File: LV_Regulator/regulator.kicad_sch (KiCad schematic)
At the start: 46 parts, among them U5 BQ25858QWRRVRQ1, U6 CSD19506KTT, U7 CSD19506KTT, U8 CSD19506KTT, U9 CSD19506KTT

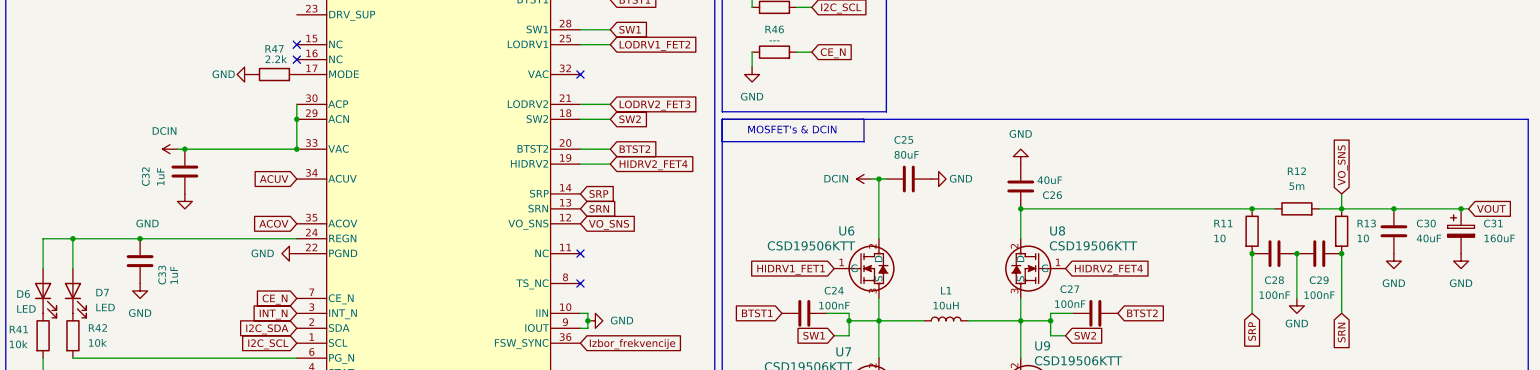
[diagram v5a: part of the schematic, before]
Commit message: Update to LV_Regulator schematic
Chosen some component's footprints as well as made a page for test points, etc.
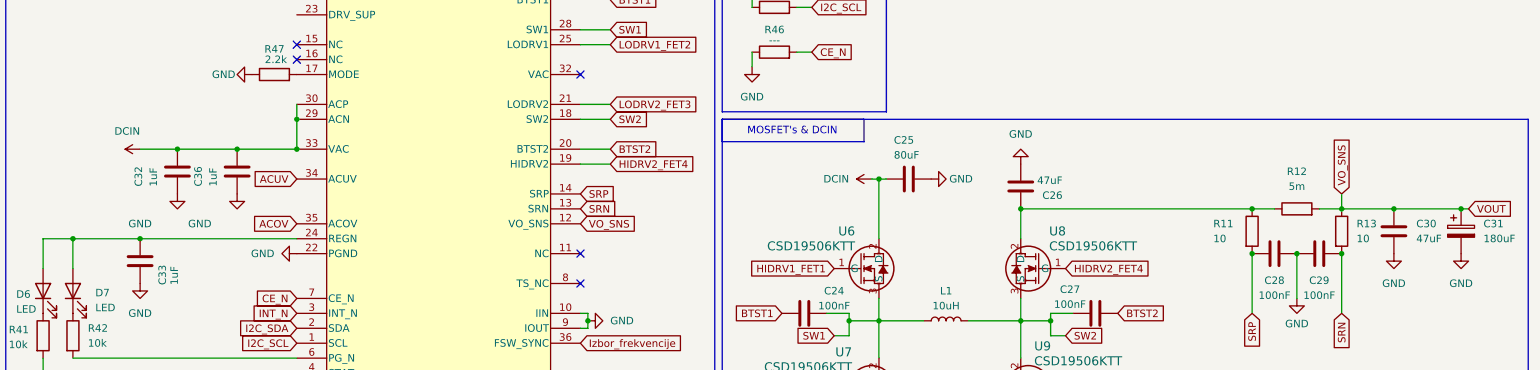
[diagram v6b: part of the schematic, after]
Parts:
- added C36: 1uF, Capacitor_SMD:C_1206_3216Metric, symbol Device:C
- C24, C27, C28: Purchase Place (none) -> https://www.digikey.com/en/products/detail/kemet/C1206C104K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
- C26, C30: value 40uF -> 47uF; footprint Capacitor_SMD:C_1206_3216Metric -> Capacitor_SMD:CP_Elec_10x10; Purchase Place (none) -> https://eu.mouser.com/ProductDetail/Vishay-BC-Components/MA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
- C29: Place of Purchase (none) -> https://www.digikey.com/en/products/detail/kemet/C1206C104K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
- C31: value 160uF -> 180uF; Buying Place (none) -> https://eu.mouser.com/ProductDetail/Nichicon/UCZ1J181MNS1MS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
- C32: Purchase place (none) -> https://eu.mouser.com/ProductDetail/KEMET/C1206C104K1RAC786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
- R12: footprint Resistor_SMD:R_1206_3216Metric -> FCSL110R005FER:RESC50110X70N; Purchase Place (none) -> https://eu.mouser.com/ProductDetail/Ohmite/FCSL110R005FER?q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
- R47: Purchase Place (none) -> https://eu.mouser.com/ProductDetail/ROHM-Semiconductor/ESR1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
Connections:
- net DCIN: now also C36.2
- net GND: now also C36.1
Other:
- moved on the sheet: C32

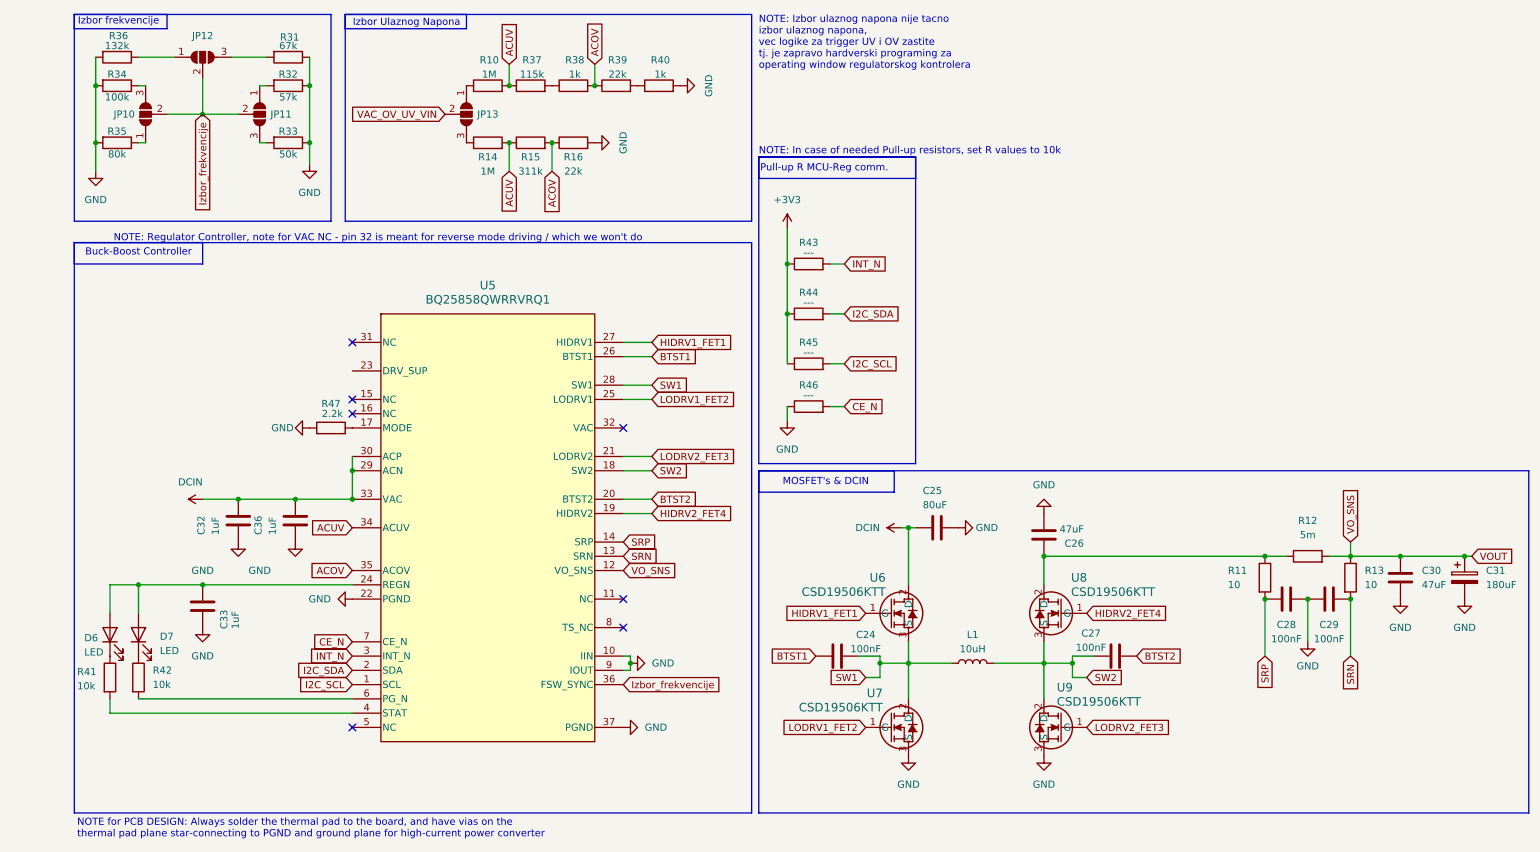
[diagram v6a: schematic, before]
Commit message: Multiple Updates
Added footprints and purchase links to the MCU page and updated some footprints on the Regulator Page from smd to SMD Handsolder
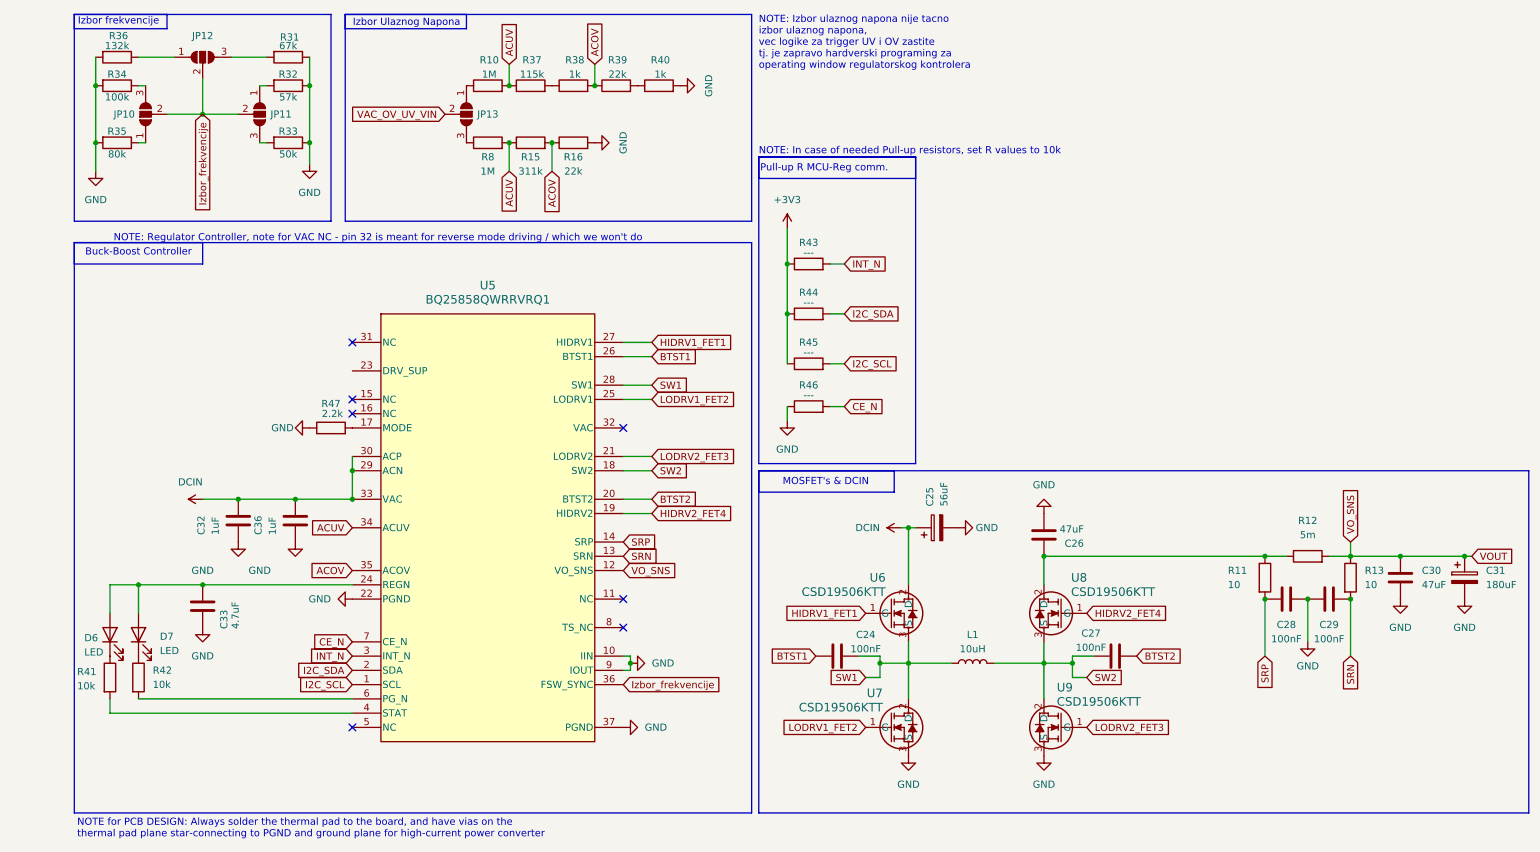
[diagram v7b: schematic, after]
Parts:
- removed C25: 80uF, Capacitor_SMD:C_1206_3216Metric, symbol Device:C
- removed R14: 1M, Resistor_SMD:R_1206_3216Metric, symbol Device:R
- added C25: 56uF, ul_UCZ1J181MNQ1MS:CAP_UCD_12P5X13P5_NCH, symbol Device:C_Polarized
- added R8: 1M, Resistor_SMD:R_1206_3216Metric_Pad1.30x1.75mm_HandSolder, symbol Device:R
- C33: value 1uF -> 4.7uF; Purchase Place (none) -> https://eu.mouser.com/ProductDetail/Walsin/SH31B475K250CT?q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
- D6, D7: Purchase Place (none) -> https://eu.mouser.com/ProductDetail/American-Bright-LED/BL-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
- JP10, JP12, JP13: footprint Jumper:SolderJumper-3_P1.3mm_Open_Pad1.0x1.5mm -> Jumper:SolderJumper-3_P1.3mm_Open_RoundedPad1.0x1.5mm
- R10, R34: footprint Resistor_SMD:R_1206_3216Metric -> Resistor_SMD:R_1206_3216Metric_Pad1.30x1.75mm_HandSolder; Purchase Place (none) -> https://eu.mouser.com/ProductDetail/KOA-Speer/RN73H2BTTD100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
- R11, R13, R47: footprint Resistor_SMD:R_1206_3216Metric -> Resistor_SMD:R_1206_3216Metric_Pad1.30x1.75mm_HandSolder
- R15: footprint Resistor_SMD:R_1206_3216Metric -> Resistor_SMD:R_1206_3216Metric_Pad1.30x1.75mm_HandSolder; Purchase Place (none) -> https://eu.mouser.com/ProductDetail/KOA-Speer/RN73H2BTTD312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
- R16, R39: footprint Resistor_SMD:R_1206_3216Metric -> Resistor_SMD:R_1206_3216Metric_Pad1.30x1.75mm_HandSolder; Purchase Place (none) -> https://eu.mouser.com/ProductDetail/KOA-Speer/RN73H2BTTD220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
- R31: footprint Resistor_SMD:R_1206_3216Metric -> Resistor_SMD:R_1206_3216Metric_Pad1.30x1.75mm_HandSolder; Purchase Place (none) -> https://eu.mouser.com/ProductDetail/KOA-Speer/RN73H2BTTD673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
- R32: footprint Resistor_SMD:R_1206_3216Metric -> Resistor_SMD:R_1206_3216Metric_Pad1.30x1.75mm_HandSolder; Purchase Place (none) -> https://eu.mouser.com/ProductDetail/KOA-Speer/RN73H2BTTD576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
- R33: footprint Resistor_SMD:R_1206_3216Metric -> Resistor_SMD:R_1206_3216Metric_Pad1.30x1.75mm_HandSolder; Purchase Place (none) -> https://eu.mouser.com/ProductDetail/KOA-Speer/RN73R2BTTD500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
- R35: footprint Resistor_SMD:R_1206_3216Metric -> Resistor_SMD:R_1206_3216Metric_Pad1.30x1.75mm_HandSolder; Purchase Place (none) -> https://eu.mouser.com/ProductDetail/KOA-Speer/RN73H2BTTD806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
- R36: footprint Resistor_SMD:R_1206_3216Metric -> Resistor_SMD:R_1206_3216Metric_Pad1.30x1.75mm_HandSolder; purchase place (none) -> https://eu.mouser.com/ProductDetail/KOA-Speer/RN73H2BTTD132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
- R37: footprint Resistor_SMD:R_1206_3216Metric -> Resistor_SMD:R_1206_3216Metric_Pad1.30x1.75mm_HandSolder; Purchase Place (none) -> https://eu.mouser.com/ProductDetail/KOA-Speer/RN73H2BTTD115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
- R38, R40: footprint Resistor_SMD:R_1206_3216Metric -> Resistor_SMD:R_1206_3216Metric_Pad1.30x1.75mm_HandSolder; Purchase Place (none) -> https://eu.mouser.com/ProductDetail/KOA-Speer/RN73R2BTTD100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
- R41: footprint Resistor_SMD:R_1206_3216Metric -> Resistor_SMD:R_1206_3216Metric_Pad1.30x1.75mm_HandSolder; Purchase Place (none) -> https://eu.mouser.com/ProductDetail/Panasonic/ERJ-T08J103V?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
- R42: footprint Resistor_SMD:R_1206_3216Metric -> Resistor_SMD:R_1206_3216Metric_Pad1.30x1.75mm_HandSolder; Purchase place (none) -> https://eu.mouser.com/ProductDetail/Panasonic/ERJ-T08J103V?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
- R43, R44, R45, R46: footprint Resistor_SMD:R_1206_3216Metric -> Resistor_SMD:R_1206_3216Metric_Pad1.30x1.75mm_HandSolder; Purchase Place (none) -> https://eu.mouser.com/ProductDetail/Vishay-Beyschlag/MCS040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
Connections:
- net ACUV: now also R8.2
- net DCIN: now also C25.1
- net GND: now also C25.2
- net at JP13.3 (B): now also R8.1

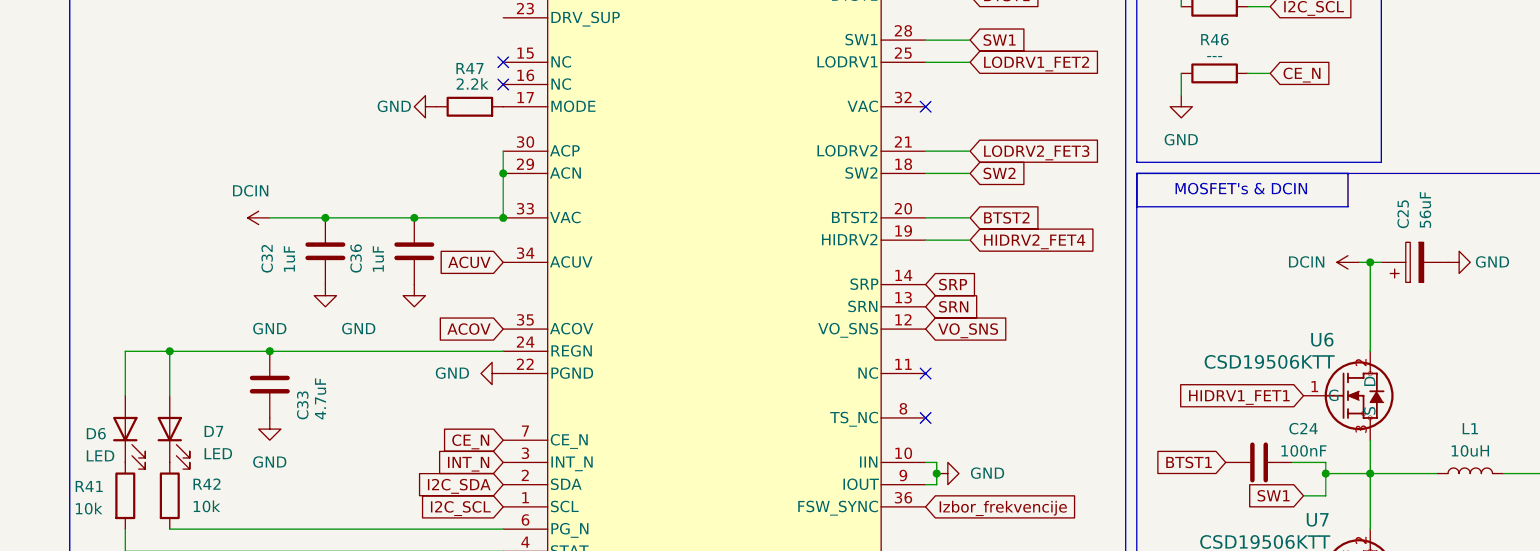
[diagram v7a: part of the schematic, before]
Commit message: Added footprints and Test points
Added test points, yet to connect them have to find where they all go exactly
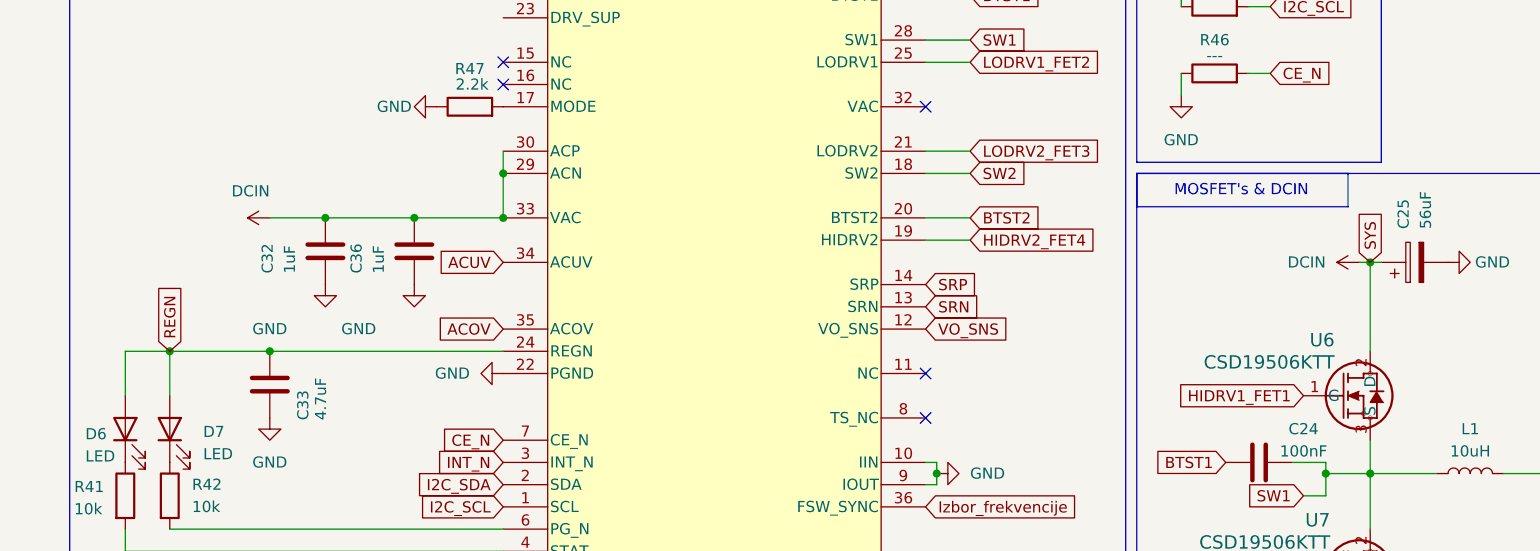
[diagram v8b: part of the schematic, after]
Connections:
- net REGN: now reaches C33.2, D6.2 (A), D7.2 (A), U5.24 (REGN)
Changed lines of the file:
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@@
+		)
+	)
+	(global_label "REGN"
+		(shape input)
+		(at 24.13 114.3 90)
+		(fields_autoplaced yes)
+		(effects
+			(font
+				(size 1.27 1.27)
+			)
+			(justify left)
+		)
+		(property "Intersheetrefs" "${INTERSHEET_REFS}"
+			(at 24.13 106.2953 90)
+			(effects
+				(font
+					(size 1.27 1.27)
+				)
+				(justify left)
+				(hide yes)
+			)
 		)
 	)
@@
 			(effects
 				(font
+					(size 1.27 1.27)
+				)
+				(justify left)
+				(hide yes)
+			)
+		)
+	)
+	(global_label "SYS"
+		(shape input)
+		(at 161.29 104.14 90)
+		(fields_autoplaced yes)
+		(effects
+			(font
+				(size 1.27 1.27)
+			)
+			(justify left)
+		)
+		(property "Intersheetrefs" "${INTERSHEET_REFS}"
+			(at 161.29 97.6472 90)
+			(effects
+				(font
